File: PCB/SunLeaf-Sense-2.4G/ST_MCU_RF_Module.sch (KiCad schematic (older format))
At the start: 17 parts, among them M1 STM32WB5MMGH6TR, SW1 B3U-1000P, T1 20021121-00010C4LF, T3 DX07S016JA1R1500, U1 USBLC6-2P6

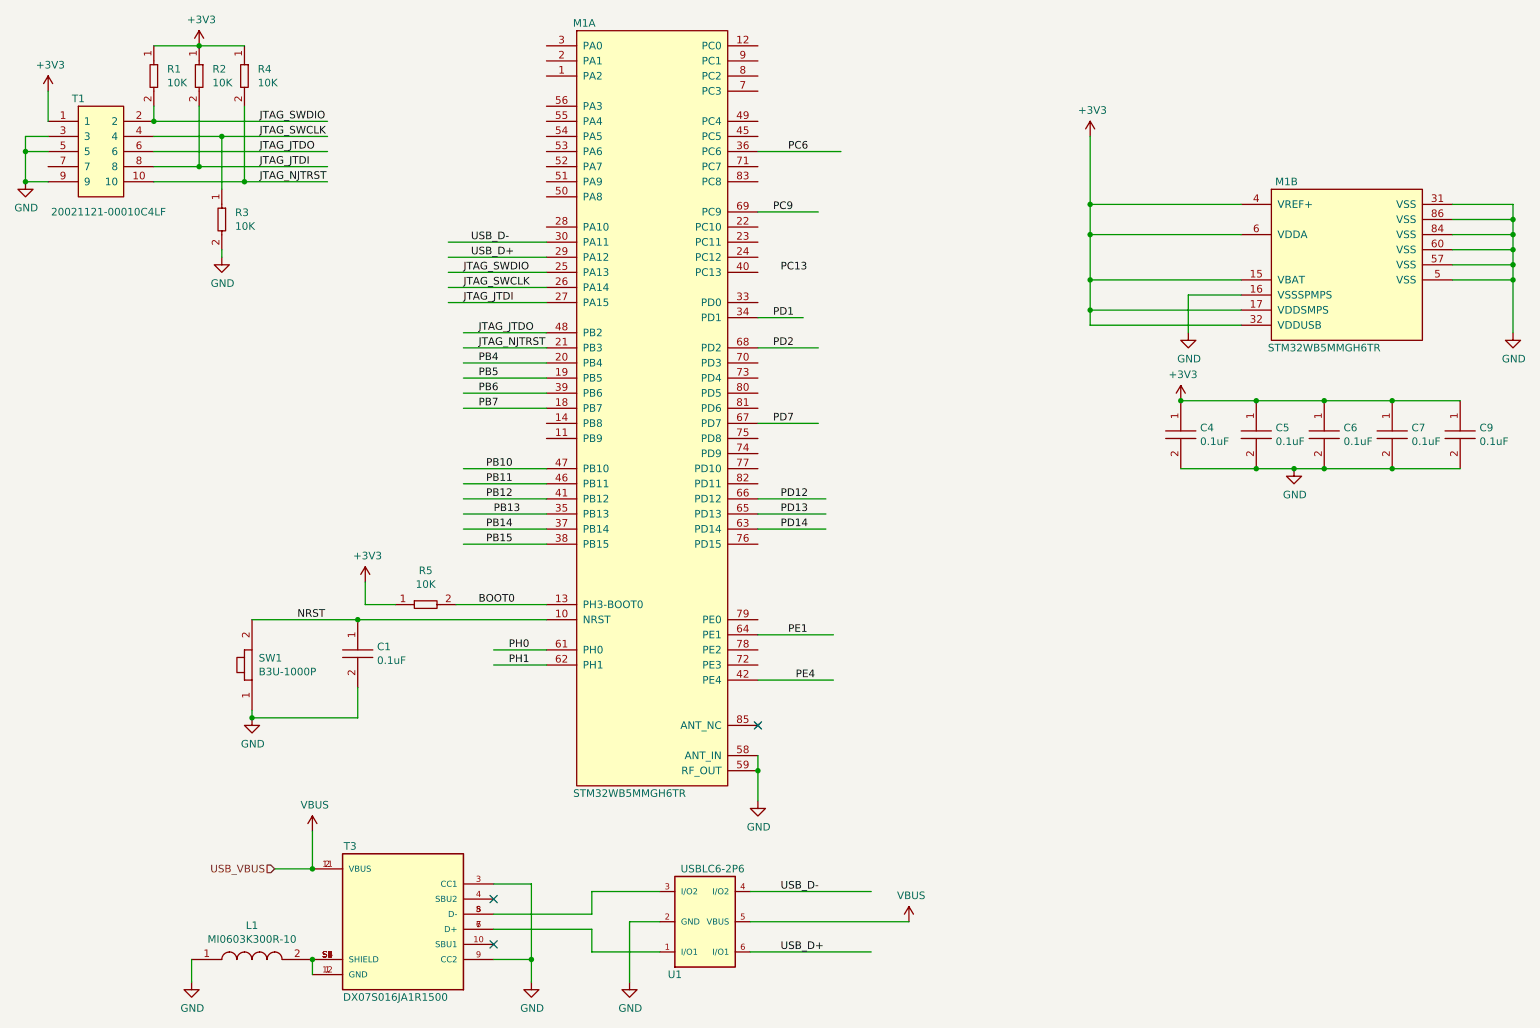
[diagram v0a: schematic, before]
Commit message: PCB
PCB started, PAR sensor circuitry integrated into design
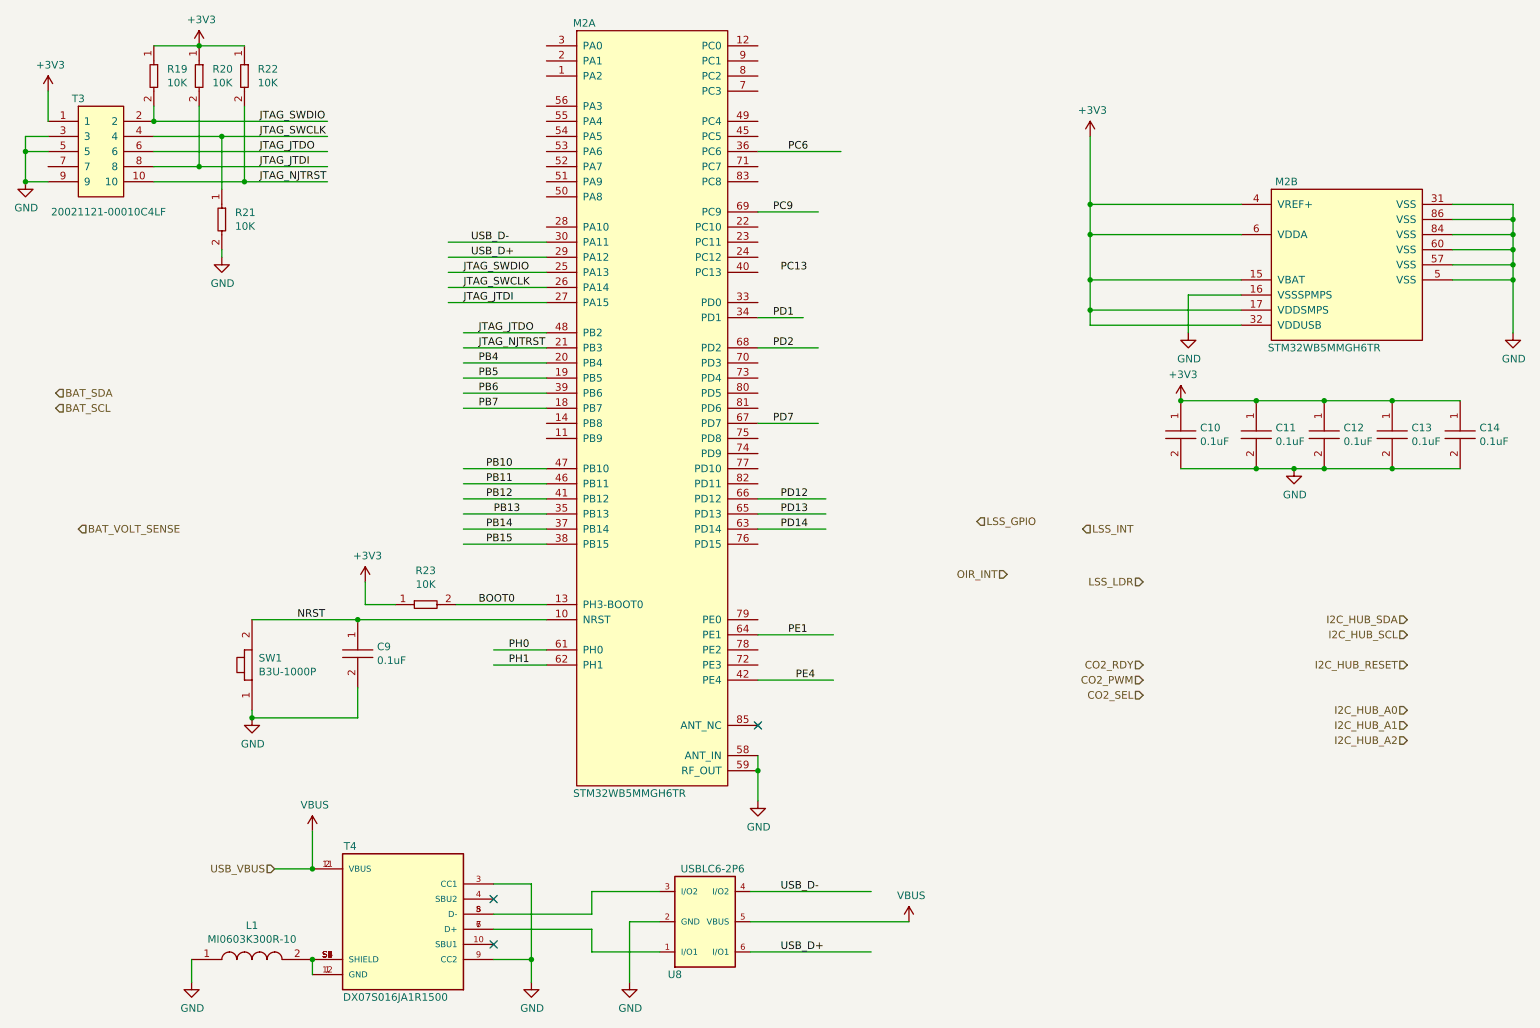
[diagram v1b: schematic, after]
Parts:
- renumbered C4 to C10, C5 to C11, C6 to C12, C7 to C13, C9 to C14, C1 to C9, M1 to M2, R1 to R19, R2 to R20, R3 to R21, R4 to R22, R5 to R23, T1 to T3, T3 to T4, U1 to U8
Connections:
- net labels added: BAT_SCL, BAT_SDA, BAT_VOLT_SENSE, CO2_PWM, CO2_RDY, CO2_SEL, I2C_HUB_A0, I2C_HUB_A1, I2C_HUB_A2, I2C_HUB_RESET, I2C_HUB_SCL, I2C_HUB_SDA, LSS_GPIO, LSS_INT, LSS_LDR, OIR_INT
